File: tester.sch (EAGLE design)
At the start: 72 parts, among them IC1 ATmega8/88/168, K1 NA 05W K, M1 SP6000C-180, P1 250, P2 10k lin, Q1 BC847CSMD, Q2 BC847CSMD, Q3 BC807-40SMD, Q4 8,000 MHz, Q5 BC847CSMD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

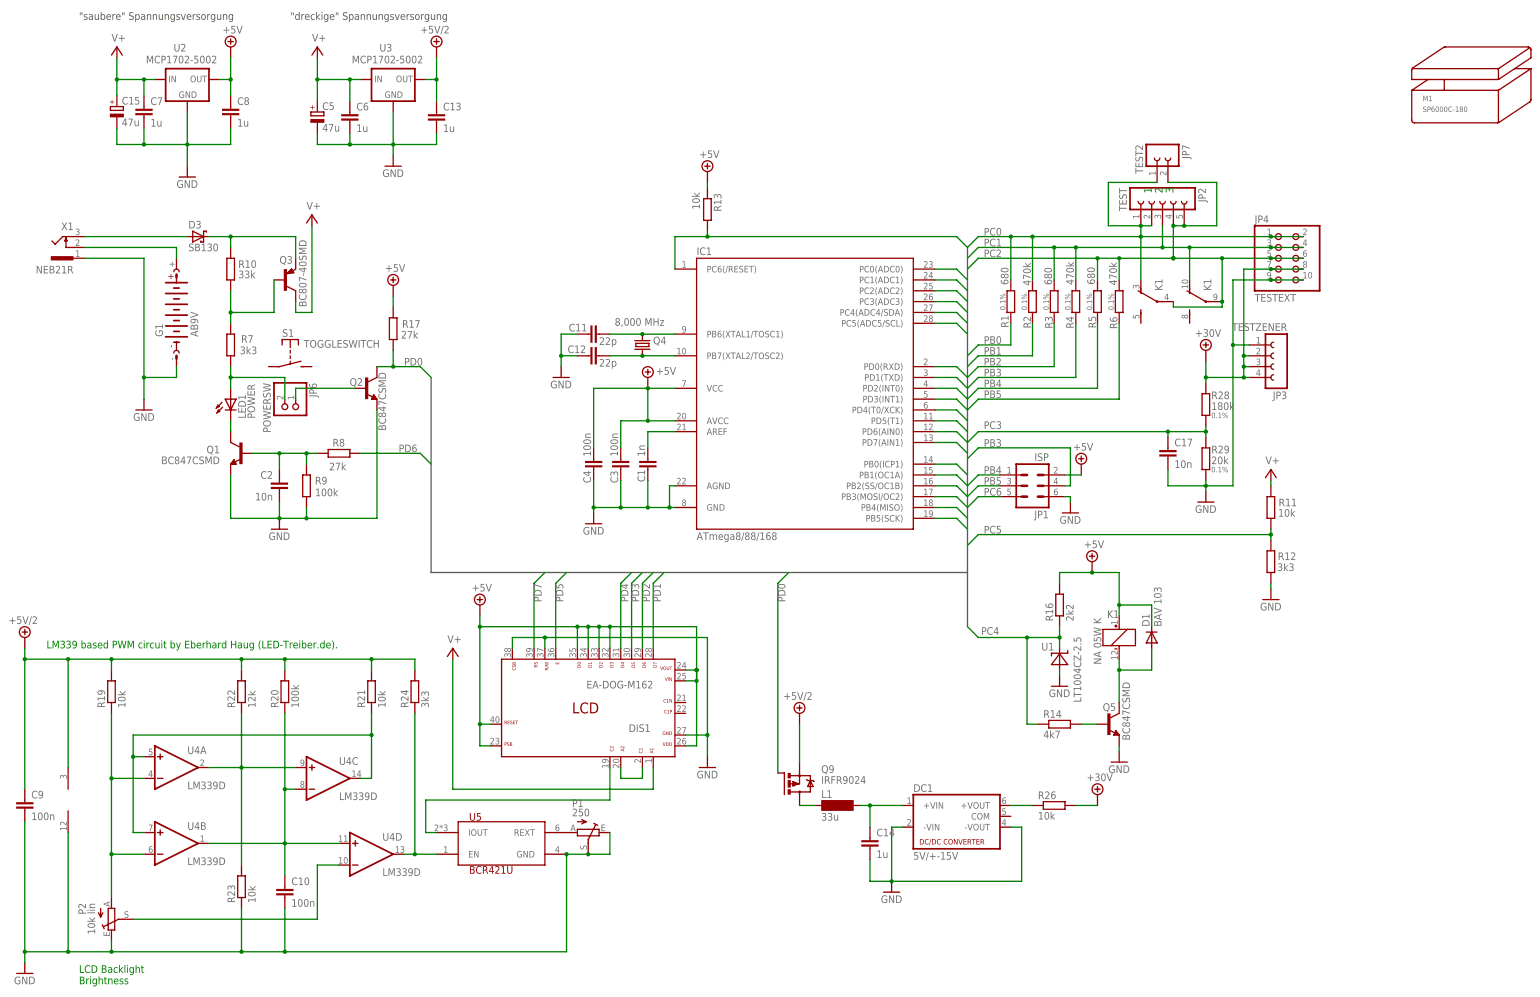
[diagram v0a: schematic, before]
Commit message: continous part names/numbers
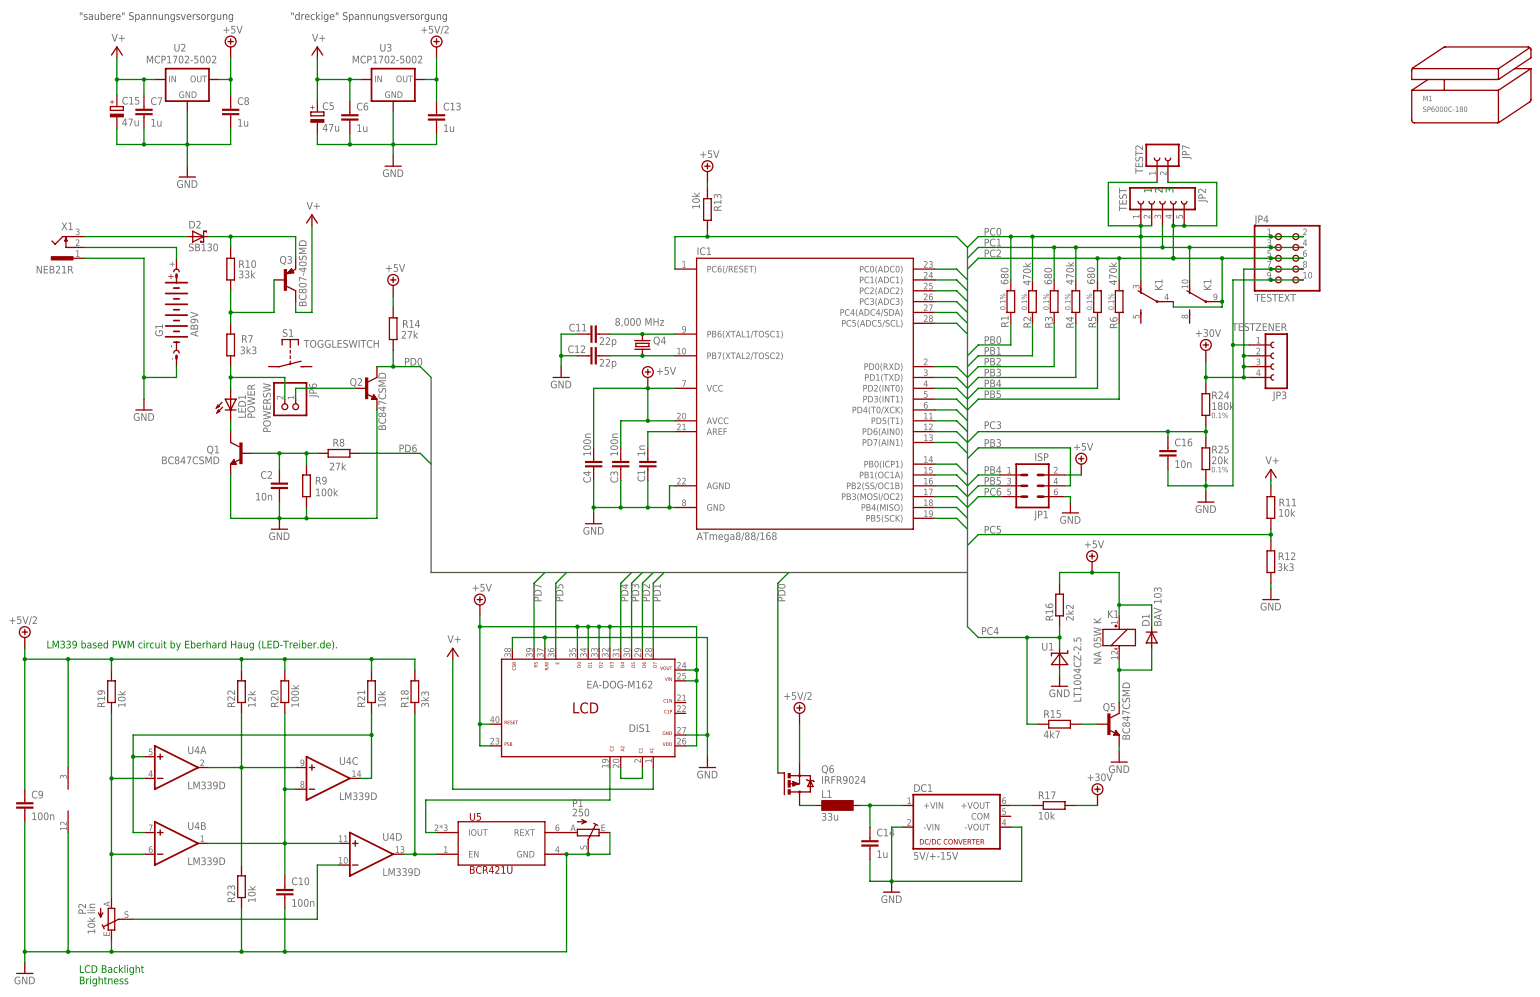
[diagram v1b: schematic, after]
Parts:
- removed R26: 10k, resistor:R-EU_R0805
- removed R28: 180k, resistor:R-EU_R0805
- added R15: 4k7, resistor:R-EU_R0805
- added R18: 3k3, resistor:R-EU_R0805
- R14: value 4k7 -> 27k
- R17: value 27k -> 10k
- R24: value 3k3 -> 180k; TOLERANCE (none) -> 0.1%
- renumbered C17 to C16, D3 to D2, Q9 to Q6, R29 to R25
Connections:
- net +30V: now also R17.2, R24.2; no longer R26.2, R28.2
- net +5V: now also R14.2; no longer R17.2
- net +5V/2: now also R18.2; no longer R24.2
- net N$17: now also R18.1; no longer R24.1
- net N$22: now also R15.2; no longer R14.2
- net N$28: now also R17.1; no longer R26.1
- net PC3: now also R24.1; no longer R28.1
- net PC4: now also R15.1; no longer R14.1
- net PD0: now also R14.1; no longer R17.1
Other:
- moved on the sheet: R14, R17, R24

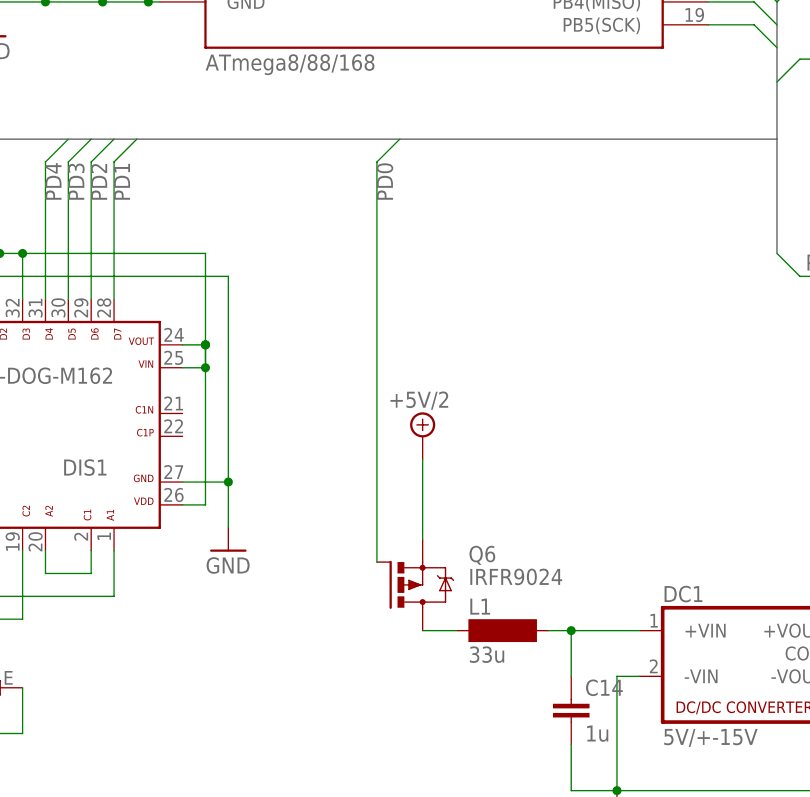
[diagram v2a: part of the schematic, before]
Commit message: IRLML 6402 for Q6
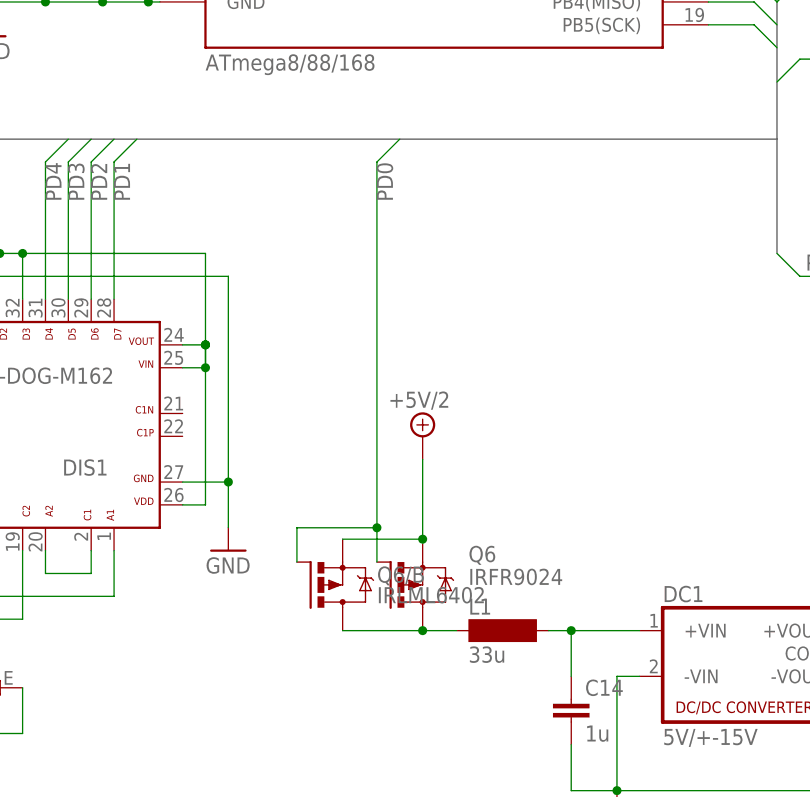
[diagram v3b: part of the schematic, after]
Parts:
- added Q6/B: IRLML6402, mosfet:IRLML6402
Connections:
- net +5V/2: now also Q6/B.S
- net N$24: now also Q6/B.D
- net PD0: now also Q6/B.G
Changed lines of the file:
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@@
 <setting verticaltext="up"/>
 </settings>
-<grid distance="0.1" unitdist="inch" unit="mm" style="lines" multiple="1" display="yes" altdistance="0.01" altunitdist="inch" altunit="mm"/>
+<grid distance="1.27" unitdist="mm" unit="mm" style="lines" multiple="1" display="yes" altdistance="635" altunitdist="mic" altunit="mic"/>
 <layers>
-<layer number="1" name="Top" color="4" fill="1" visible="yes" active="no"/>
-<layer number="2" name="Route2" color="1" fill="3" visible="yes" active="no"/>
-<layer number="3" name="Route3" color="4" fill="3" visible="yes" active="no"/>
-<layer number="4" name="Route4" color="1" fill="4" visible="yes" active="no"/>
-<layer number="5" name="Route5" color="4" fill="4" visible="yes" active="no"/>
-<layer number="6" name="Route6" color="1" fill="8" visible="yes" active="no"/>
-<layer number="7" name="Route7" color="4" fill="8" visible="yes" active="no"/>
-<layer number="8" name="Route8" color="1" fill="2" visible="yes" active="no"/>
-<layer number="9" name="Route9" color="4" fill="2" visible="yes" active="no"/>
-<layer number="10" name="Route10" color="1" fill="7" visible="yes" active="no"/>
-<layer number="11" name="Route11" color="4" fill="7" visible="yes" active="no"/>
-<layer number="12" name="Route12" color="1" fill="5" visible="yes" active="no"/>
-<layer number="13" name="Route13" color="4" fill="5" visible="yes" active="no"/>
-<layer number="14" name="Route14" color="1" fill="6" visible="yes" active="no"/>
-<layer number="15" name="Route15" color="4" fill="6" visible="yes" active="no"/>
-<layer number="16" name="Bottom" color="1" fill="1" visible="yes" active="no"/>
-<layer number="17" name="Pads" color="2" fill="1" visible="yes" active="no"/>
-<layer number="18" name="Vias" color="2" fill="1" visible="yes" active="no"/>
-<layer number="19" name="Unrouted" color="22" fill="1" visible="yes" active="no"/>
-<layer number="20" name="Dimension" color="15" fill="1" visible="yes" active="no"/>
-<layer number="21" name="tPlace" color="7" fill="1" visible="yes" active="no"/>
-<layer number="22" name="bPlace" color="7" fill="1" visible="yes" active="no"/>
-<layer number="23" name="tOrigins" color="15" fill="1" visible="yes" active="no"/>
-<layer number="24" name="bOrigins" color="15" fill="1" visible="yes" active="no"/>
-<layer number="25" name="tNames" color="7" fill="1" visible="yes" active="no"/>
-<layer number="26" name="bNames" color="7" fill="1" visible="yes" active="no"/>
-<layer number="27" name="tValues" color="7" fill="1" visible="yes" active="no"/>
-<layer number="28" name="bValues" color="7" fill="1" visible="yes" active="no"/>
+<layer number="1" name="Top" color="4" fill="1" visible="no" active="no"/>
+<layer number="2" name="Route2" color="1" fill="3" visible="no" active="no"/>
+<layer number="3" name="Route3" color="4" fill="3" visible="no" active="no"/>
+<layer number="4" name="Route4" color="1" fill="4" visible="no" active="no"/>
+<layer number="5" name="Route5" color="4" fill="4" visible="no" active="no"/>
+<layer number="6" name="Route6" color="1" fill="8" visible="no" active="no"/>
+<layer number="7" name="Route7" color="4" fill="8" visible="no" active="no"/>
+<layer number="8" name="Route8" color="1" fill="2" visible="no" active="no"/>
+<layer number="9" name="Route9" color="4" fill="2" visible="no" active="no"/>
+<layer number="10" name="Route10" color="1" fill="7" visible="no" active="no"/>
+<layer number="11" name="Route11" color="4" fill="7" visible="no" active="no"/>
+<layer number="12" name="Route12" color="1" fill="5" visible="no" active="no"/>
+<layer number="13" name="Route13" color="4" fill="5" visible="no" active="no"/>
+<layer number="14" name="Route14" color="1" fill="6" visible="no" active="no"/>
+<layer number="15" name="Route15" color="4" fill="6" visible="no" active="no"/>
+<layer number="16" name="Bottom" color="1" fill="1" visible="no" active="no"/>
+<layer number="17" name="Pads" color="2" fill="1" visible="no" active="no"/>
+<layer number="18" name="Vias" color="2" fill="1" visible="no" active="no"/>
+<layer number="19" name="Unrouted" color="22" fill="1" visible="no" active="no"/>
+<layer number="20" name="Dimension" color="15" fill="1" visible="no" active="no"/>
+<layer number="21" name="tPlace" color="7" fill="1" visible="no" active="no"/>
+<layer number="22" name="bPlace" color="7" fill="1" visible="no" active="no"/>
+<layer number="23" name="tOrigins" color="15" fill="1" visible="no" active="no"/>
+<layer number="24" name="bOrigins" color="15" fill="1" visible="no" active="no"/>
+<layer number="25" name="tNames" color="7" fill="1" visible="no" active="no"/>
+<layer number="26" name="bNames" color="7" fill="1" visible="no" active="no"/>
+<layer number="27" name="tValues" color="7" fill="1" visible="no" active="no"/>
+<layer number="28" name="bValues" color="7" fill="1" visible="no" active="no"/>
 <layer number="29" name="tStop" color="7" fill="3" visible="no" active="no"/>
 <layer number="30" name="bStop" color="7" fill="6" visible="no" active="no"/>
@@
 <layer number="35" name="tGlue" color="7" fill="4" visible="no" active="no"/>
 <layer number="36" name="bGlue" color="7" fill="5" visible="no" active="no"/>
-<layer number="37" name="tTest" color="7" fill="1" visible="yes" active="no"/>
-<layer number="38" name="bTest" color="7" fill="1" visible="yes" active="no"/>
+<layer number="37" name="tTest" color="7" fill="1" visible="no" active="no"/>
+<layer number="38" name="bTest" color="7" fill="1" visible="no" active="no"/>
 <layer number="39" name="tKeepout" color="4" fill="11" visible="no" active="no"/>
 <layer number="40" name="bKeepout" color="1" fill="11" visible="no" active="no"/>
@@
 <layer number="44" name="Drills" color="7" fill="1" visible="no" active="no"/>
 <layer number="45" name="Holes" color="7" fill="1" visible="no" active="no"/>
-<layer number="46" name="Milling" color="3" fill="1" visible="yes" active="no"/>
-<layer number="47" name="Measures" color="7" fill="1" visible="yes" active="no"/>
-<layer number="48" name="Document" color="7" fill="1" visible="yes" active="no"/>
-<layer number="49" name="Reference" color="7" fill="1" visible="yes" active="no"/>
-<layer number="50" name="dxf" color="7" fill="1" visible="yes" active="no"/>
-<layer number="51" name="tDocu" color="7" fill="1" visible="yes" active="no"/>
-<layer number="52" name="bDocu" color="7" fill="1" visible="yes" active="no"/>
-<layer number="53" name="tPadExt" color="7" fill="1" visible="yes" active="no"/>
-<layer number="54" name="bPadExt" color="1" fill="1" visible="yes" active="no"/>
+<layer number="46" name="Milling" color="3" fill="1" visible="no" active="no"/>
+<layer number="47" name="Measures" color="7" fill="1" visible="no" active="no"/>
+<layer number="48" name="Document" color="7" fill="1" visible="no" active="no"/>
+<layer number="49" name="Reference" color="7" fill="1" visible="no" active="no"/>
+<layer number="50" name="dxf" color="7" fill="1" visible="no" active="no"/>
+<layer number="51" name="tDocu" color="7" fill="1" visible="no" active="no"/>
+<layer number="52" name="bDocu" color="7" fill="1" visible="no" active="no"/>
+<layer number="53" name="tPadExt" color="7" fill="1" visible="no" active="no"/>
+<layer number="54" name="bPadExt" color="1" fill="1" visible="no" active="no"/>
 <layer number="91" name="Nets" color="2" fill="1" visible="yes" active="yes"/>
 <layer number="92" name="Busses" color="1" fill="1" visible="yes" active="yes"/>
@@
 <part name="SUPPLY5" library="supply2" deviceset="V+" device=""/>
 <part name="GND12" library="supply1" deviceset="GND" device=""/>
+<part name="Q6/B" library="mosfet" deviceset="IRLML6402" device=""/>
 </parts>
 <sheets>
@@
 <instance part="SUPPLY5" gate="1" x="118.11" y="111.76"/>
 <instance part="GND12" gate="1" x="274.32" y="85.09"/>
+<instance part="Q6/B" gate="G$1" x="187.96" y="80.01"/>
 </instances>
 <busses>
@@
 <segment>
 <pinref part="Q6" gate="G$1" pin="G"/>
-<wire x1="194.31" y1="127" x2="194.31" y2="82.55" width="0.1524" layer="91"/>
+<wire x1="194.31" y1="127" x2="194.31" y2="86.36" width="0.1524" layer="91"/>
 <label x="194.31" y="127" size="1.778" layer="95" rot="R270"/>
+<wire x1="194.31" y1="86.36" x2="194.31" y2="82.55" width="0.1524" layer="91"/>
 <wire x1="196.85" y1="129.54" x2="194.31" y2="127" width="0.1524" layer="91"/>
+<pinref part="Q6/B" gate="G$1" pin="G"/>
+<wire x1="185.42" y1="82.55" x2="185.42" y2="86.36" width="0.1524" layer="91"/>
+<wire x1="185.42" y1="86.36" x2="194.31" y2="86.36" width="0.1524" layer="91"/>
+<junction x="194.31" y="86.36"/>
 </segment>
 </net>
@@
 <wire x1="199.39" y1="74.93" x2="203.2" y2="74.93" width="0.1524" layer="91"/>
 <pinref part="L1" gate="G$1" pin="1"/>
+<pinref part="Q6/B" gate="G$1" pin="D"/>
+<wire x1="190.5" y1="74.93" x2="199.39" y2="74.93" width="0.1524" layer="91"/>
+<junction x="199.39" y="74.93"/>
 </segment>
 </net>
@@
 <pinref part="SUPPLY6" gate="G$1" pin="+5V/2"/>
 <wire x1="199.39" y1="93.98" x2="199.39" y2="85.09" width="0.1524" layer="91"/>
-</segment>
-<segment>
+<pinref part="Q6/B" gate="G$1" pin="S"/>
+<wire x1="190.5" y1="85.09" x2="199.39" y2="85.09" width="0.1524" layer="91"/>
+<junction x="199.39" y="85.09"/>
+</segment>
+<segment>
